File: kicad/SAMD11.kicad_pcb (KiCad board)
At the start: 2 copper layers, 57 parts, among them J1 USB_OTG, J10 CONN_PA03, J11 CONN_PA02, J12 CONN_GND, J13 CONN_5V, J14 CONN_3V, J15 CONN_RST, J17 CONN_PA23, J18 CONN_PA22, J19 CONN_PA17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

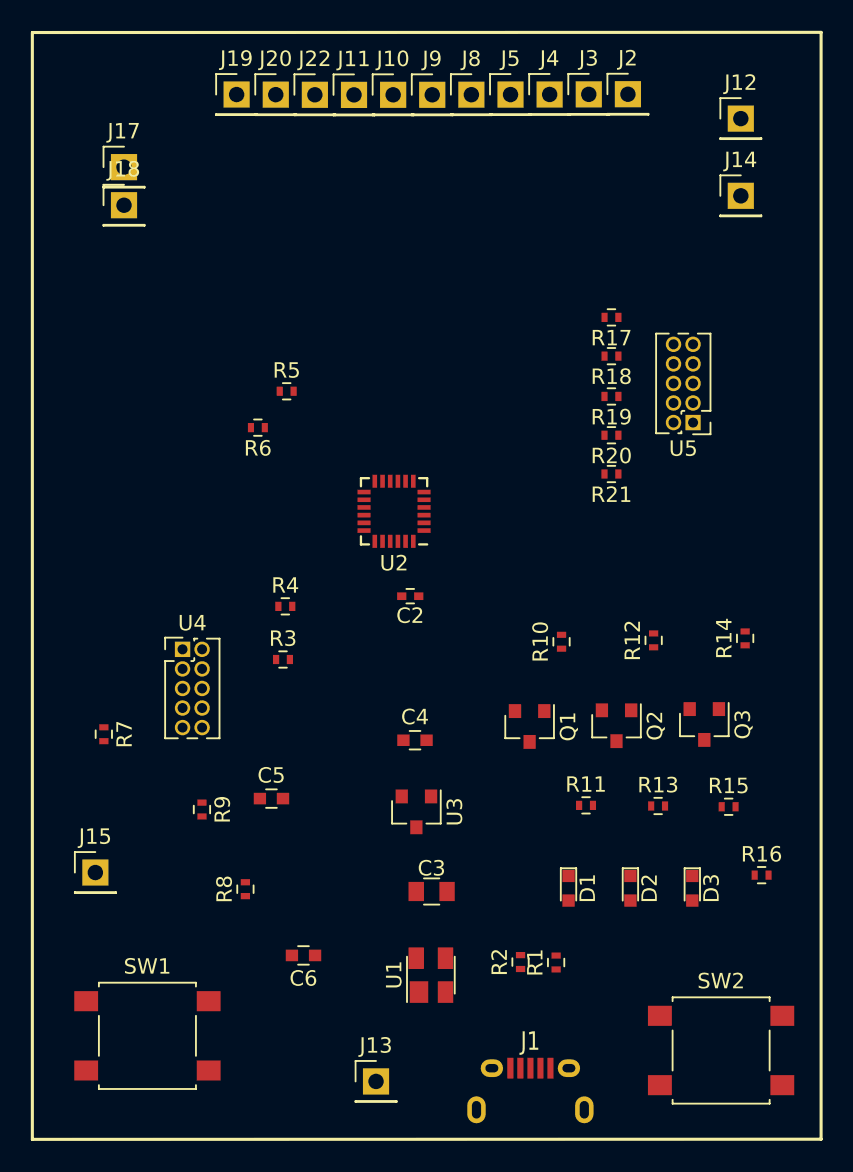
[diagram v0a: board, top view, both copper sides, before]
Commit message: Finished preliminary board layout
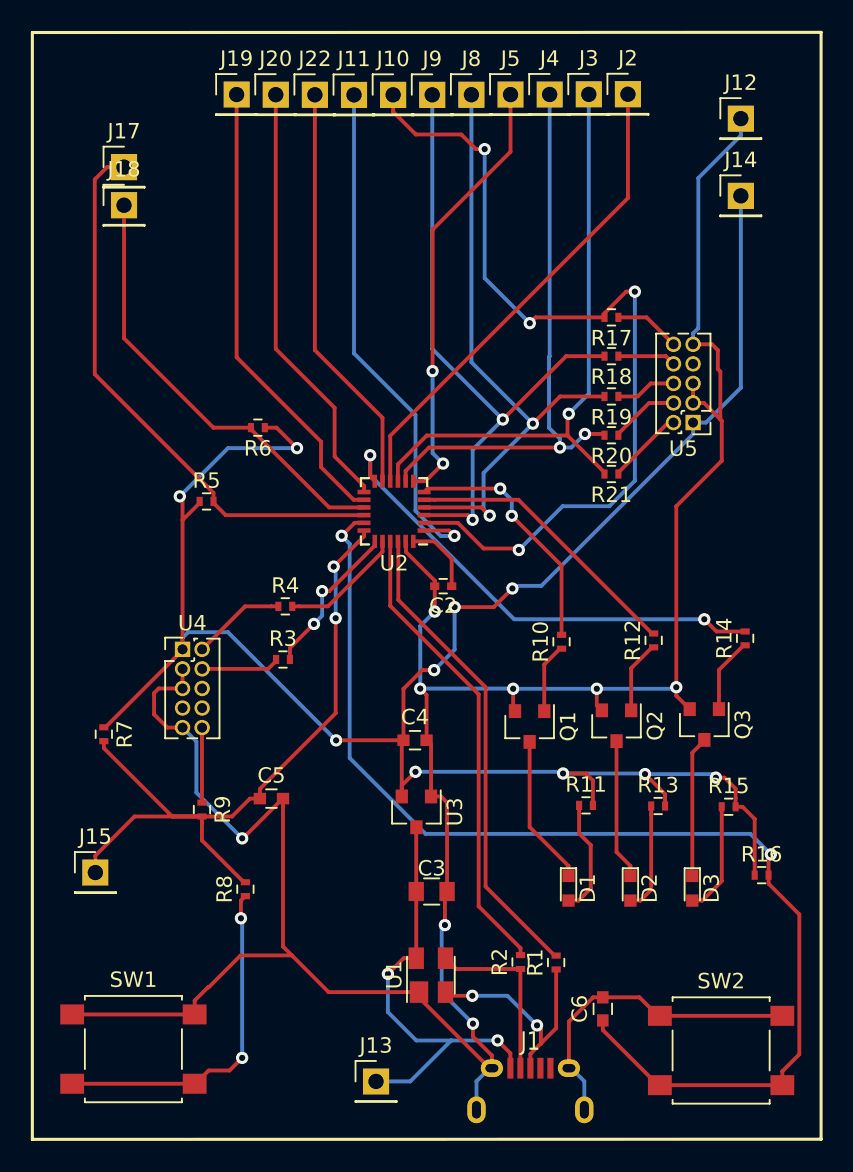
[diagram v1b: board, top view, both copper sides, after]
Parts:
- moved C6 19.7 mm to (116.8, 140.0), turned to 90 degrees
- moved R5 8.84 mm to (91.1, 107.0)
- moved C2 2.24 mm to (106.4, 112.5)
- moved SW1 1.25 mm to (86.3, 142.6)
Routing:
- net GND: track 0.00 -> 190.6 mm, vias 0 -> 8
- net +3V3: track 0.00 -> 140.8 mm, vias 0 -> 10
- net AT_PA27: track 0.00 -> 76.4 mm, vias 0 -> 2
- net AT_PA03: track 0.00 -> 56.9 mm, vias 0 -> 4
- net AT_RST: track 0.00 -> 47.8 mm, vias 0 -> 2
- net AT_PA04: track 0.00 -> 41.9 mm, vias 0 -> 2
- net AT_PA05: track 0.00 -> 40.3 mm, vias 0 -> 2
- net AT_PA10: track 0.00 -> 39.1 mm, vias 0 -> 1
- net AT_PA09: track 0.00 -> 37.8 mm, vias 0 -> 2
- net AT_PA23: track 0.00 -> 36.5 mm
- net AT_PA02: track 0.00 -> 34.0 mm, vias 0 -> 1
- net AT_PA15: track 0.00 -> 31.7 mm, vias 0 -> 2
- net AT_PA11: track 0.00 -> 31.5 mm
- net Net-(R1-Pad2): track 0.00 -> 31.2 mm
- net Net-(R2-Pad2): track 0.00 -> 30.4 mm
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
